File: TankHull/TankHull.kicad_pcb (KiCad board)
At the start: 2 copper layers, 80.8 x 44 mm, 62 parts, among them J1 SlipRing_6, J10 Conn_01x02_Socket, J2 Conn_01x02_Socket, J3 Conn_01x02_Socket, J4 Conn_01x02_Socket, J5 Conn_01x02_Socket, J7 Conn_01x05, J8 Conn_01x02_Socket, J9 Conn_01x02_Socket, Q1 Q_PMOS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

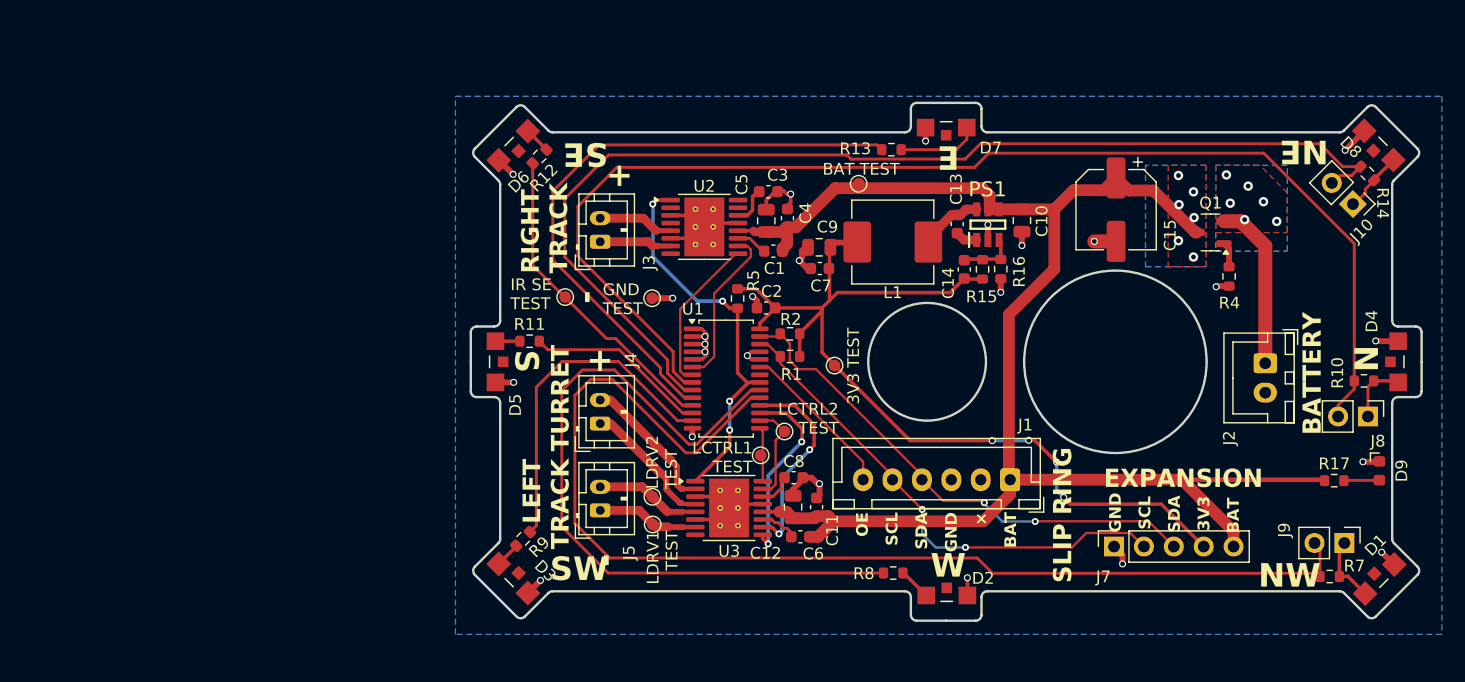
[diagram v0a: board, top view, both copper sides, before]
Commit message: began IR receiver update on hull board
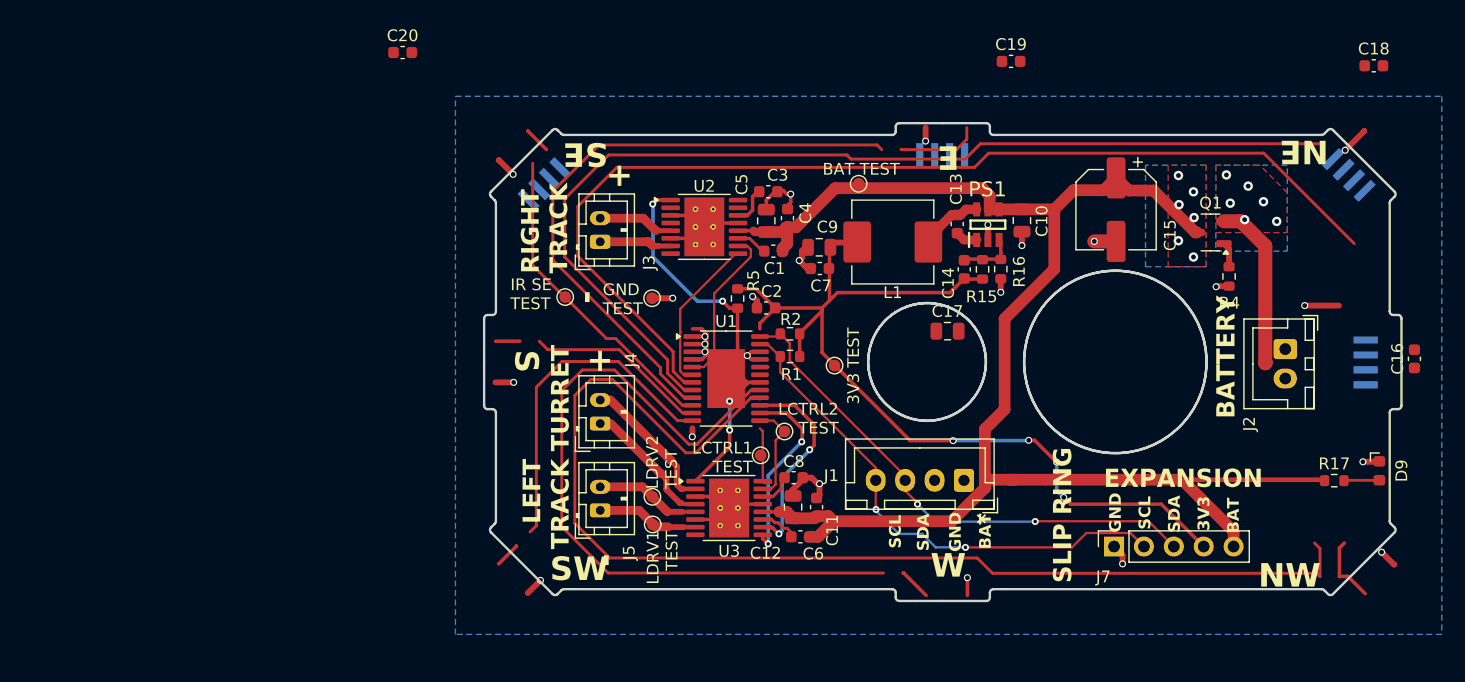
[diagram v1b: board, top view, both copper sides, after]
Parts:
- removed D1, D2, D3, D4, D5, D6, D7, D8: VSMB10940, Thundergeddon:DIO_VSMB10940
- removed J10, J8, J9: Conn_01x02_Socket, Connector_PinHeader_2.54mm:PinHeader_1x02_P2.54mm_Vertical
- removed R10, R11, R12, R13, R14, R7, R8, R9: 330RΩ, Resistor_SMD:R_0603_1608Metric
- added C16: 100nF, Capacitor_SMD:C_0603_1608Metric, F.Cu at (158.2, 102.4)
- added C17: 47uF, Capacitor_SMD:C_0805_2012Metric, F.Cu at (118.5, 100.0)
- added C18: 100nF, Capacitor_SMD:C_0603_1608Metric, F.Cu at (154.7, 77.5)
- added C19: 100nF, Capacitor_SMD:C_0603_1608Metric, F.Cu at (123.9, 77.1)
- added C20: 100nF, Capacitor_SMD:C_0603_1608Metric, F.Cu at (72.2, 76.3)
- added U4: TSSP77038TR, Vishay IR receiver:TSSP77038TR_VIS, B.Cu at (154.6, 102.7)
- added U5: TSSP77038TR, Vishay IR receiver:TSSP77038TR_VIS, B.Cu at (153.0, 86.3)
- added U6: TSSP77038TR, Vishay IR receiver:TSSP77038TR_VIS, B.Cu at (118.0, 84.5)
- added U7: TSSP77038TR, Vishay IR receiver:TSSP77038TR_VIS, B.Cu at (83.8, 87.1)
- J1: value SlipRing_6 -> SlipRing_4; footprint Connector_JST:JST_XH_B6B-XH-A_1x06_P2.50mm_Vertical -> Connector_JST:JST_XH_B4B-XH-A_1x04_P2.50mm_Vertical
- U1: value PCA9685PW -> PCA9555PW; footprint Package_SO:TSSOP-28_4.4x9.7mm_P0.65mm -> Package_SO:TSSOP-24-1EP_4.4x7.8mm_P0.65mm_EP3.2x5mm
- moved J1 3.93 mm to (119.9, 112.7)
- moved J2 2.08 mm to (147.2, 101.5)
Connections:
- net /IR Transmit SE renamed /IR Receive SE
- U1 pad 10: /IR Transmit E -> /IR Receive E
- U1 pad 8: /IR Transmit N -> /IR Receive N
- U1 pad 9: /IR Transmit NE -> /IR Receive NE
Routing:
- net /IR Transmit N: track 105.7 -> 0.00 mm
- net /IR Transmit NE: track 94.8 -> 0.00 mm
- net /Right Motor Control 2: track 13.3 -> 103.7 mm
- net /IR Receive N: track 0.00 -> 87.5 mm
- net /IR Transmit E: track 52.6 -> 0.00 mm
- net /IR Receive NE: track 0.00 -> 52.6 mm
- net (no net): track 0.00 -> 49.2 mm
- net /IR Transmit SW: track 28.8 -> 0.00 mm
- net /OE: track 13.6 -> 0.00 mm
- net /IR Transmit S: track 15.5 -> 28.8 mm
- net /IR Receive SE: track 27.2 -> 15.5 mm
- net Net-(D7-PadA): track 6.94 -> 0.00 mm
- net Net-(J9-Pin_1): track 5.83 -> 0.00 mm
- net Net-(J8-Pin_1): track 5.35 -> 0.00 mm
- net Net-(J10-Pin_1): track 5.25 -> 0.00 mm
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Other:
- board size 80.8 x 44 mm -> 77.9 x 40.6 mm
- board text removed: "N"
- board text removed: "OE"

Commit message: continue with ir receiver update
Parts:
- removed C2: 100nF, Capacitor_SMD:C_0603_1608Metric
- removed R1, R2: 3.3kΩ, Resistor_SMD:R_0603_1608Metric
- removed R5: 10kΩ, Resistor_SMD:R_0603_1608Metric
- removed TP3, TP4, TP5: TestPoint, TestPoint:TestPoint_Pad_D1.0mm
- removed U1: PCA9555PW, Package_SO:TSSOP-24-1EP_4.4x7.8mm_P0.65mm_EP3.2x5mm
- added C21: 100nF, Capacitor_SMD:C_0603_1608Metric, F.Cu at (41.7, 100.5)
- added C22: 100nF, Capacitor_SMD:C_0603_1608Metric, F.Cu at (41.7, 103.0)
- added C23: 100nF, Capacitor_SMD:C_0603_1608Metric, F.Cu at (41.7, 105.5)
- added C24: 100nF, Capacitor_SMD:C_0603_1608Metric, F.Cu at (41.7, 108.0)
- added C25: 100nF, Capacitor_SMD:C_0603_1608Metric, F.Cu at (41.7, 110.5)
- added R10: 10kΩ, Resistor_SMD:R_0603_1608Metric, F.Cu at (45.7, 108.0)
- added R11: 10kΩ, Resistor_SMD:R_0603_1608Metric, F.Cu at (45.7, 110.5)
- added R13: 10kΩ, Resistor_SMD:R_0603_1608Metric, F.Cu at (45.7, 113.0)
- added R14: 10kΩ, Resistor_SMD:R_0603_1608Metric, F.Cu at (49.8, 100.5)
- added R18: 10kΩ, Resistor_SMD:R_0603_1608Metric, F.Cu at (49.8, 103.0)
- added R19: 10kΩ, Resistor_SMD:R_0603_1608Metric, F.Cu at (49.8, 105.5)
- added R3: 3.3kΩ, Resistor_SMD:R_0603_1608Metric, F.Cu at (41.7, 113.0)
- added R7: 3.3kΩ, Resistor_SMD:R_0603_1608Metric, F.Cu at (45.7, 100.5)
- added R8: 10kΩ, Resistor_SMD:R_0603_1608Metric, F.Cu at (45.7, 103.0)
- added R9: 10kΩ, Resistor_SMD:R_0603_1608Metric, F.Cu at (45.7, 105.5)
- added U10: TSSP77038TR, Vishay IR receiver:TSSP77038TR_VIS, B.Cu at (83.9, 118.2)
- added U11: TSSP77038TR, Vishay IR receiver:TSSP77038TR_VIS, B.Cu at (118.1, 120.7)
- added U12: TSSP77038TR, Vishay IR receiver:TSSP77038TR_VIS, B.Cu at (152.3, 118.2)
- added U8: PCA9555PW, Package_SO:TSSOP-24_4.4x7.8mm_P0.65mm, F.Cu at (58.6, 114.2)
- added U9: TSSP77038TR, Vishay IR receiver:TSSP77038TR_VIS, B.Cu at (81.4, 102.7)
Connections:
- C16 pad 2: Net-(U4-VS) -> +3V3_HULL
- C17 pad 1: Net-(U4-VS) -> GND
- C18 pad 1: Net-(U5-GND) -> GND
- C18 pad 2: Net-(U5-VS) -> +3V3_HULL
- C19 pad 1: Net-(U6-GND) -> GND
- C19 pad 2: Net-(U6-VS) -> +3V3_HULL
- C20 pad 1: Net-(U7-GND) -> GND
- C20 pad 2: Net-(U7-VS) -> +3V3_HULL
- U4 pad 2: Net-(U4-VS) -> +3V3_HULL
- U5 pad 1: Net-(U5-GND) -> GND
- U5 pad 2: Net-(U5-VS) -> +3V3_HULL
- U6 pad 1: Net-(U6-GND) -> GND
- U6 pad 2: Net-(U6-VS) -> +3V3_HULL
- U7 pad 1: Net-(U7-GND) -> GND
- U7 pad 2: Net-(U7-VS) -> +3V3_HULL
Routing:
- net (no net): track 49.2 -> 241.3 mm
- net /IR Transmit NW: track 100.0 -> 0.00 mm
- net /IR Transmit W: track 63.3 -> 0.00 mm
- net /IR Transmit S: track 28.8 -> 0.00 mm

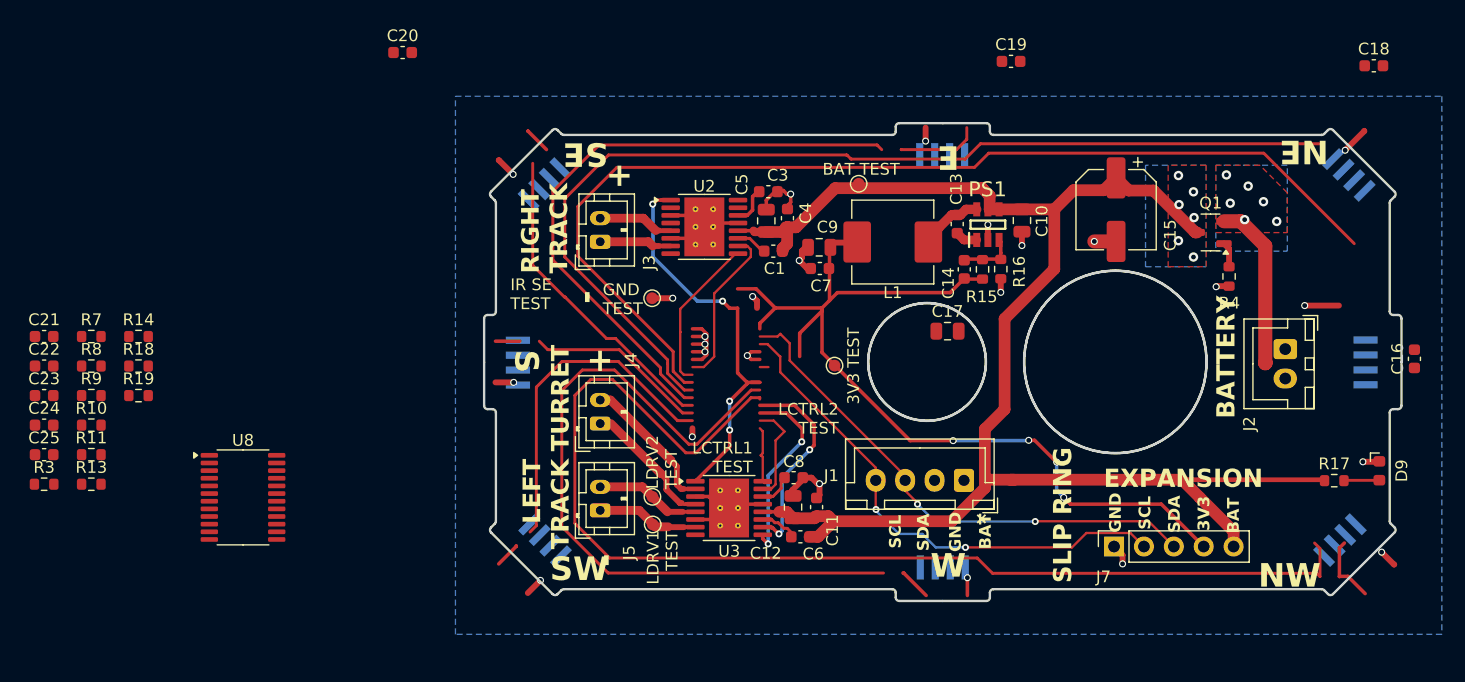
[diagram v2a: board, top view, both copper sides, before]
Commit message: continued with IR receiver update
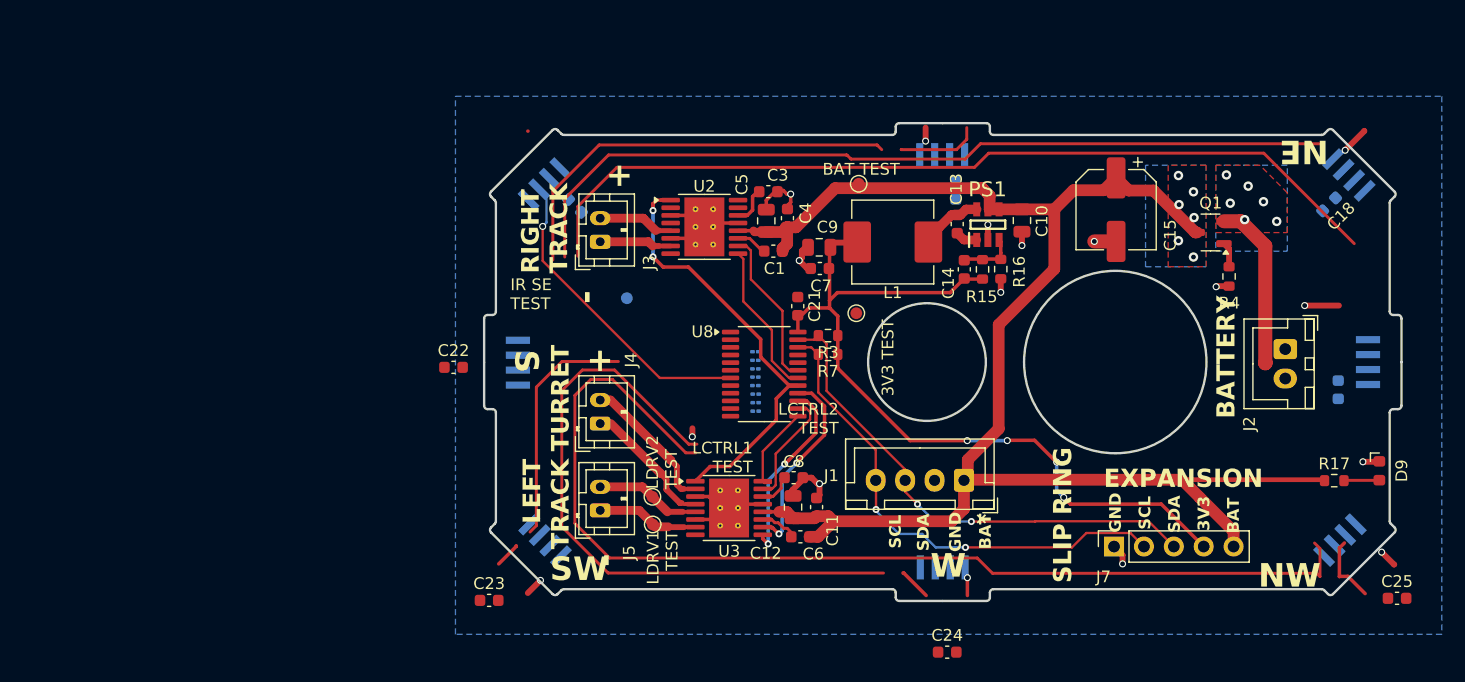
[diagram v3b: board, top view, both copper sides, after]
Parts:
- removed C17: 47uF, Capacitor_SMD:C_0805_2012Metric
- C16, C18, C19, C20, TP8: moved to B.Cu
- R10, R11, R13, R14, R18, R19, R8, R9: footprint Resistor_SMD:R_0603_1608Metric -> Resistor_SMD:R_01005_0402Metric; moved to B.Cu
- moved C25 115.6 mm to (156.7, 122.7)
- moved C24 79.1 mm to (118.5, 127.3)
- moved R3 67.8 mm to (108.3, 100.4), turned to 180 degrees
- moved C21 64.1 mm to (105.8, 97.9), turned to -90 degrees
- moved R7 62.6 mm to (108.3, 102.0), turned to 180 degrees
- moved R13 57.3 mm to (102.2, 103.2)
- moved R11 56.6 mm to (102.2, 106.1), turned to 180 degrees
- moved R9 56.5 mm to (102.2, 102.5)
- moved R10 56.5 mm to (102.2, 106.8), turned to 180 degrees
- moved R8 56.4 mm to (102.2, 101.8)
- moved R14 52.5 mm to (102.2, 103.9)
- moved R18 52.5 mm to (102.2, 105.4), turned to 180 degrees
- moved R19 52.4 mm to (102.2, 104.7), turned to 180 degrees
- moved U8 45.5 mm to (102.9, 103.7)
- moved C23 41.6 mm to (79.5, 122.9)
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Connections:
- J1 pad 2: unconnected-(J1-Pin_2-Pad2) -> GND
- J1 pad 3: GND -> /SDA
- J1 pad 4: /SDA -> /SCL
- U8 pad 13: /Right Motor Control 1 -> /Left Motor Control 1
- U8 pad 14: /Right Motor Control 2 -> /Left Motor Control 2
- U8 pad 15: /Left Motor Control 1 -> /Turret Motor Control 1
- U8 pad 16: /Left Motor Control 2 -> /Turret Motor Control 2
- U8 pad 17: /Turret Motor Control 1 -> /Motors Sleep
- U8 pad 18: /Turret Motor Control 2 -> /Right Motor Control 2
- U8 pad 19: /Motors Sleep -> /Right Motor Control 1
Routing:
- net (no net): track 241.3 -> 38.1 mm
- net /Left Motor Control 1: track 5.54 -> 100.1 mm
- net /Right Motor Control 2: track 103.7 -> 13.1 mm
- net /IR Receive N: track 87.5 -> 0.00 mm
- net /IR Receive SE: track 15.5 -> 101.8 mm, vias 0 -> 1
- net +3V3_HULL: track 82.5 -> 142.6 mm
- net /Left Motor Control 2: track 8.54 -> 65.2 mm
- net /IR Receive NE: track 52.6 -> 0.00 mm
- net /IR Receive W: track 0.00 -> 35.6 mm
- net GND: track 69.4 -> 53.1 mm, vias 25 -> 17
- net /Motors Sleep: track 34.8 -> 38.6 mm, vias 4 -> 2
- net /SCL: track 43.9 -> 42.5 mm
- net +BATT: track 133.2 -> 134.5 mm
- net /SDA: track 44.2 -> 43.0 mm
- net /Turret Motor Control 2: track 17.4 -> 16.8 mm
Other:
- outline, holes or cut-outs redrawn

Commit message: submit before using cleanup tool
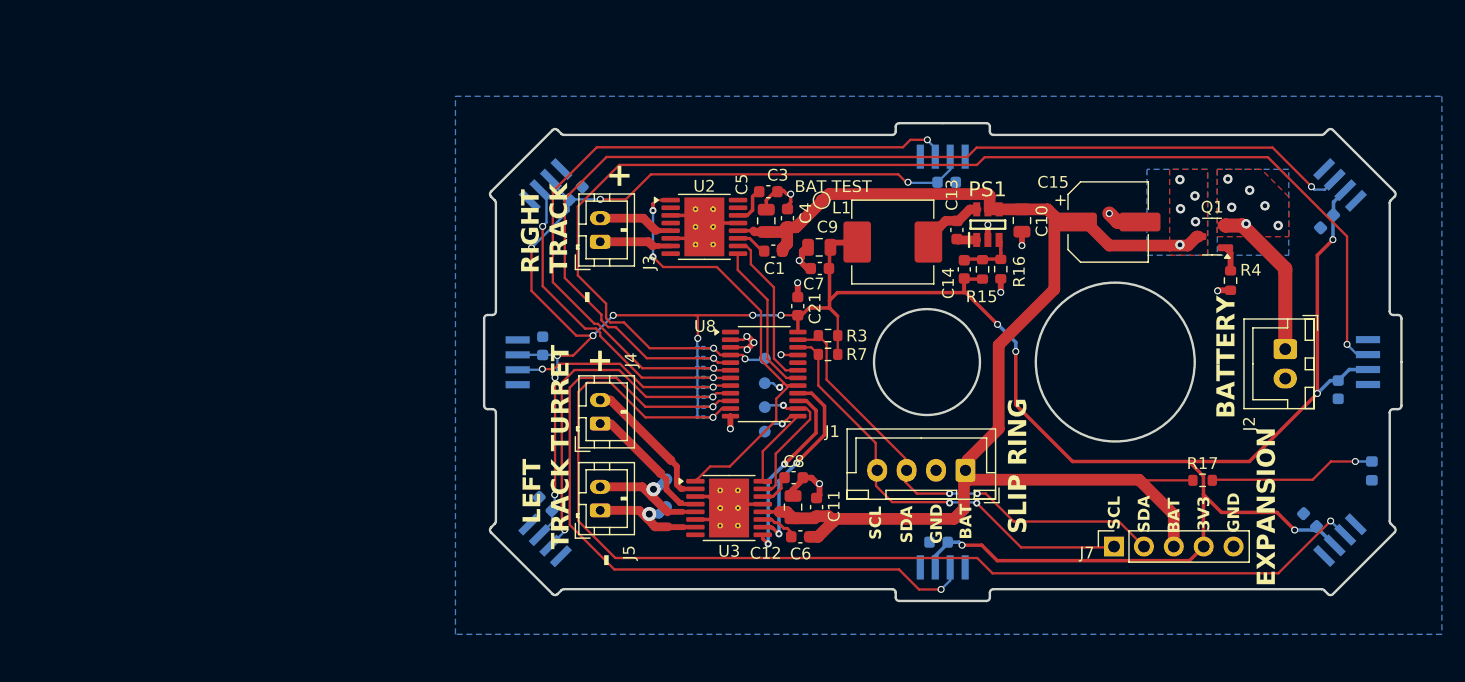
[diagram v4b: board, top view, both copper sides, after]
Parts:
- removed TP2, TP8: TestPoint, TestPoint:TestPoint_Pad_D1.0mm
- added IR N TST: TestPoint_Pad_D1.0mm, TestPoint:TestPoint_Pad_D1.0mm, B.Cu at (103.0, 102.4)
- added LM1 TST: TestPoint_Pad_D1.0mm, TestPoint:TestPoint_Pad_D1.0mm, B.Cu at (103.0, 108.6)
- added LM2 TST: TestPoint_Pad_D1.0mm, TestPoint:TestPoint_Pad_D1.0mm, B.Cu at (103.0, 106.5)
- added MS TST: TestPoint_Pad_D1.0mm, TestPoint:TestPoint_Pad_D1.0mm, B.Cu at (103.0, 104.4)
- C22, C23, C24, C25, D9, TP6, TP7: moved to B.Cu
- moved R17 11.2 mm to (140.2, 112.7)
- moved C25 9.95 mm to (149.3, 116.1), turned to -45 degrees
- moved C23 9.50 mm to (84.3, 114.7), turned to -45 degrees
- moved C24 9.37 mm to (117.7, 118.0)
- moved C22 7.79 mm to (84.1, 101.3), turned to -90 degrees
- moved R10 4.73 mm to (97.5, 107.3)
- moved R11 4.69 mm to (97.5, 106.5)
- moved R8 4.69 mm to (97.5, 101.4)
- moved R18 4.68 mm to (97.5, 105.6)
- moved R9 4.68 mm to (97.5, 102.3)
- moved R19 4.68 mm to (97.5, 104.8)
- moved R13 4.68 mm to (97.5, 103.1)
- moved R14 4.68 mm to (97.5, 104.0)
- moved TP1 3.45 mm to (107.8, 88.9)
- moved TP7 1.90 mm to (94.6, 112.6)
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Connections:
- J7 pad 1: GND -> /SCL
- J7 pad 2: /SCL -> /SDA
- J7 pad 3: /SDA -> +BATT
- J7 pad 5: +BATT -> GND
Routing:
- net /IR Receive N: track 0.00 -> 108.0 mm, vias 0 -> 3
- net +3V3_HULL: track 142.6 -> 247.6 mm, vias 4 -> 17
- net /IR Receive NW: track 0.00 -> 95.9 mm, vias 0 -> 2
- net /IR Receive NE: track 0.00 -> 94.0 mm, vias 0 -> 2
- net /Left Motor Control 1: track 100.1 -> 10.9 mm, vias 0 -> 1
- net /IR Receive SE: track 101.8 -> 28.8 mm, vias 1 -> 2
- net /IR Receive E: track 0.00 -> 62.2 mm, vias 0 -> 2
- net /Left Motor Control 2: track 65.2 -> 12.9 mm, vias 0 -> 1
- net (no net): track 38.1 -> 0.00 mm
- net /IR Receive SW: track 0.00 -> 31.1 mm, vias 0 -> 2
- net /IR Receive W: track 35.6 -> 63.7 mm, vias 0 -> 2
- net /IR Receive S: track 0.00 -> 20.0 mm, vias 0 -> 2
- net +BATT: track 134.5 -> 120.2 mm, vias 6 -> 5
- net Net-(D9-A): track 3.08 -> 14.3 mm, vias 0 -> 1
- net /SCL: track 42.5 -> 37.7 mm
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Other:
- outline, holes or cut-outs redrawn
- board text added: "LD1 TST"
- board text added: "LD2 TST"
- board text added: "N"
- board text added: "THUNDERGEDDON"
- board text added: "v0.2"
- board text removed: "3V3 TEST"
- board text removed: "GND TEST"
- board text removed: "IR SE TEST"
- board text removed: "LCTRL1 TEST"
- board text removed: "LCTRL2 TEST"
- board text removed: "LDRV1 TEST"
- board text removed: "LDRV2 TEST"
- board text removed: "×"
